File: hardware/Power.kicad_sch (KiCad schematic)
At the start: 70 parts, among them J10 I2C, J3 ESTOP, J4 PWR, J5 Conn_ARM_JTAG_SWD_10, J7 FAN, J9 DEBUG, Q1 MMBT5401LT1G, Q2 PSMN4R8-100BSEJ, Q3 MMBT3904, Q5 PSMN4R8-100BSEJ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

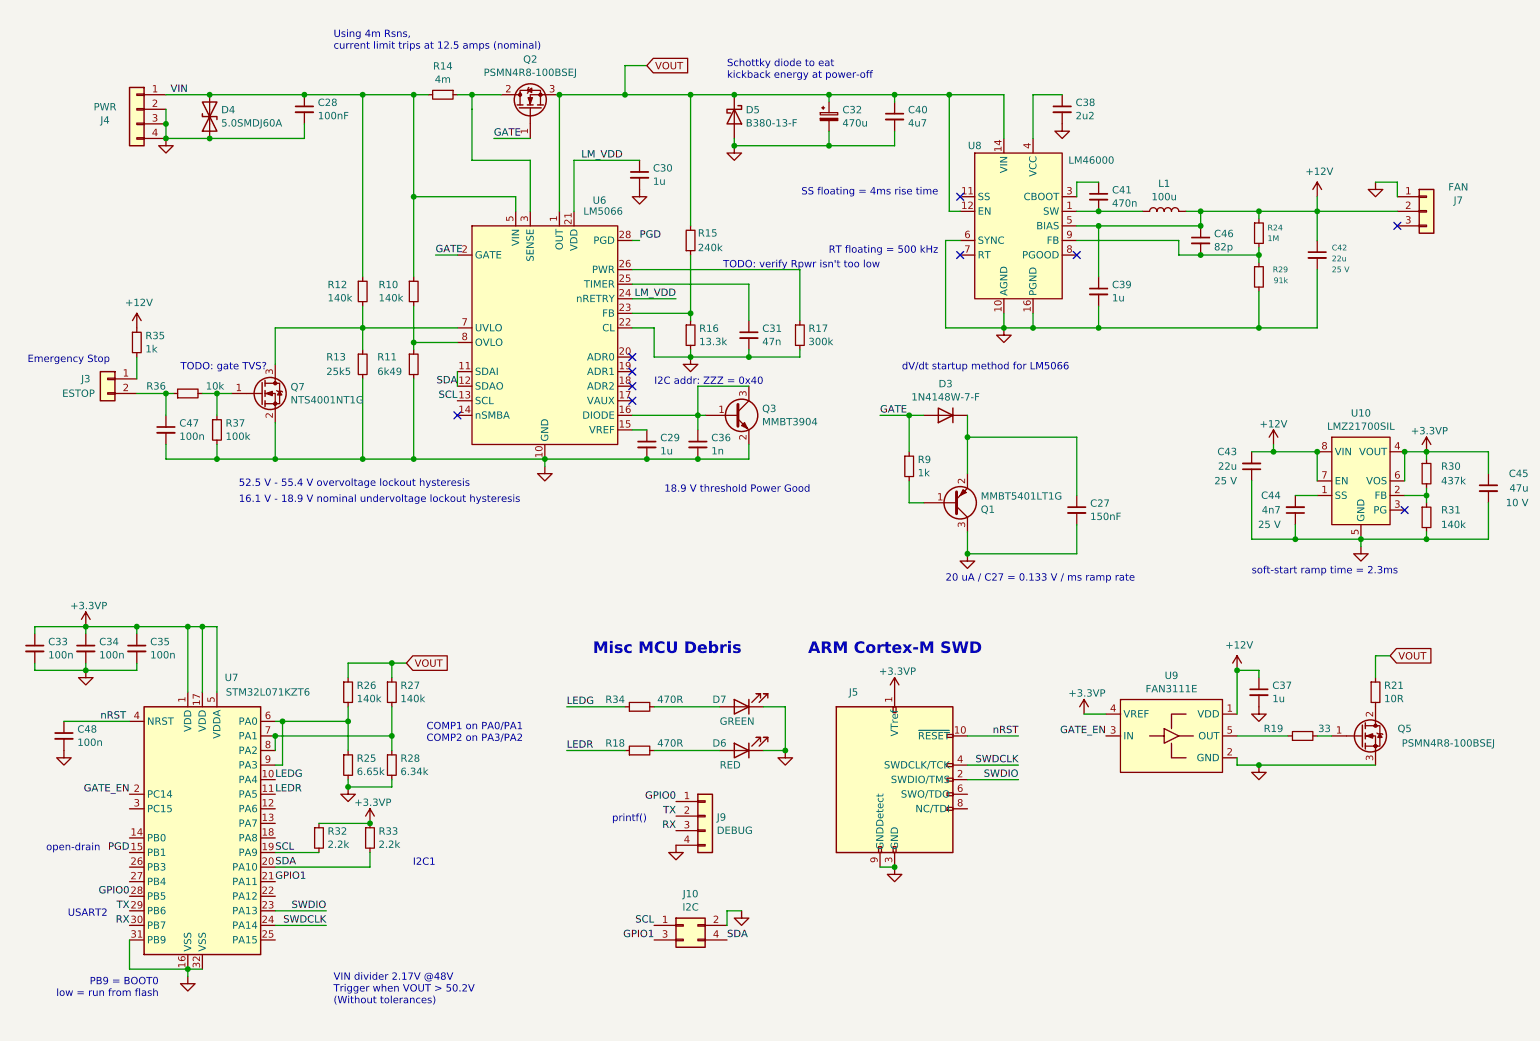
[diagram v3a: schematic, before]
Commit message: 12V rail supplied off of VIN and Shunt EN switched to a clockable pin.
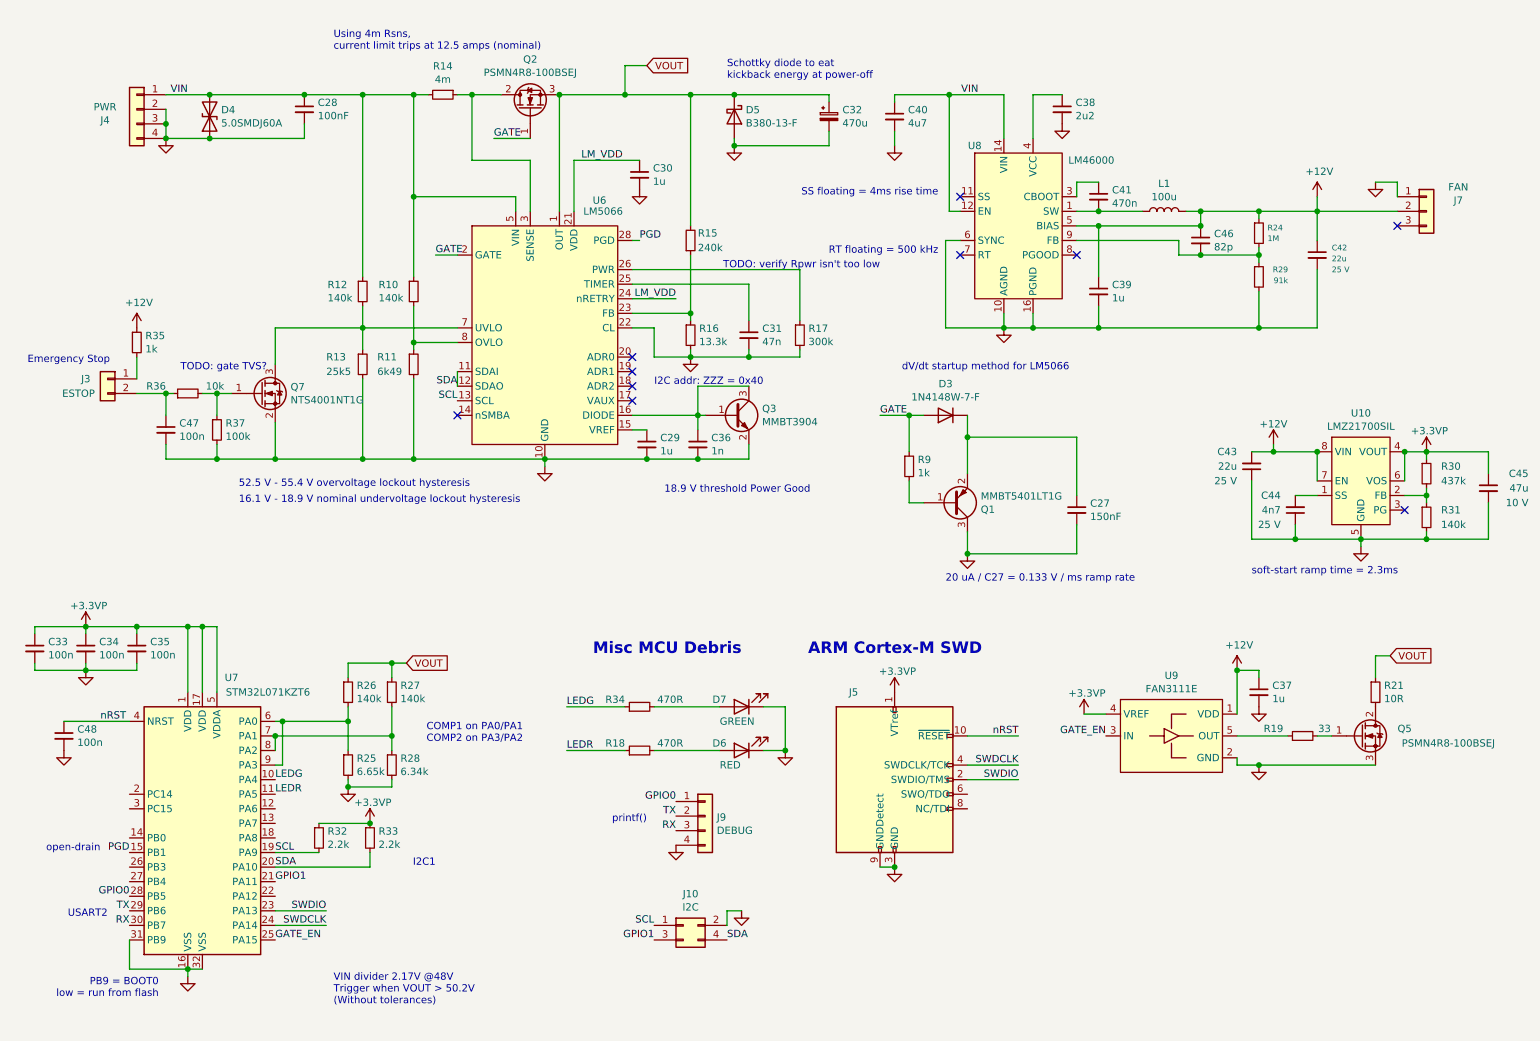
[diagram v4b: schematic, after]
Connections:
- net GATE_EN: now also U7.25 (PA15); no longer U7.2 (PC14)
- net VIN: now also C40.1, U8.12 (EN), U8.13 (VIN), U8.14 (VIN)
- net VOUT: no longer C40.1, U8.12 (EN), U8.13 (VIN), U8.14 (VIN)
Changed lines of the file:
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@@
   (junction (at 140.97 73.66) (diameter 1.016) (color 0 0 0 0))
   (junction (at 147.32 142.24) (diameter 1.016) (color 0 0 0 0))
-  (junction (at 154.94 27.94) (diameter 1.016) (color 0 0 0 0))
-  (junction (at 154.94 36.83) (diameter 1.016) (color 0 0 0 0))
-  (junction (at 166.37 27.94) (diameter 1.016) (color 0 0 0 0))
   (junction (at 166.37 162.56) (diameter 1.016) (color 0 0 0 0))
   (junction (at 168.91 83.82) (diameter 1.016) (color 0 0 0 0))
@@
   (junction (at 259.08 97.79) (diameter 1.016) (color 0 0 0 0))
   (junction (at 259.08 105.41) (diameter 1.016) (color 0 0 0 0))
-  (no_connect (at 254 50.8))
   (no_connect (at 90.17 83.82))
   (no_connect (at 255.27 100.33))
+  (no_connect (at 177.8 55.88))
+  (no_connect (at 254 50.8))
+  (no_connect (at 177.8 45.72))
   (no_connect (at 198.12 55.88))
   (no_connect (at 120.65 73.66))
+  (no_connect (at 120.65 78.74))
   (no_connect (at 120.65 76.2))
   (no_connect (at 120.65 81.28))
-  (no_connect (at 120.65 78.74))
-  (no_connect (at 177.8 55.88))
-  (no_connect (at 177.8 45.72))
   (wire (pts (xy 16.51 120.65) (xy 25.4 120.65))
     (stroke (width 0) (type solid) (color 0 0 0 0))
@@
     (stroke (width 0) (type solid) (color 0 0 0 0))
   )
-  (wire (pts (xy 92.71 27.94) (xy 92.71 30.48))
+  (wire (pts (xy 92.71 27.94) (xy 92.71 39.37))
     (stroke (width 0) (type solid) (color 0 0 0 0))
   )
@@
     (stroke (width 0) (type solid) (color 0 0 0 0))
   )
-  (wire (pts (xy 92.71 30.48) (xy 92.71 39.37))
-    (stroke (width 0) (type solid) (color 0 0 0 0))
-  )
   (wire (pts (xy 92.71 39.37) (xy 102.87 39.37))
     (stroke (width 0) (type solid) (color 0 0 0 0))
@@
     (stroke (width 0) (type solid) (color 0 0 0 0))
   )
-  (wire (pts (xy 154.94 27.94) (xy 166.37 27.94))
-    (stroke (width 0) (type solid) (color 0 0 0 0))
-  )
   (wire (pts (xy 154.94 34.29) (xy 154.94 36.83))
     (stroke (width 0) (type solid) (color 0 0 0 0))
@@
     (stroke (width 0) (type solid) (color 0 0 0 0))
   )
-  (wire (pts (xy 154.94 36.83) (xy 166.37 36.83))
-    (stroke (width 0) (type solid) (color 0 0 0 0))
-  )
   (wire (pts (xy 163.83 162.56) (xy 166.37 162.56))
     (stroke (width 0) (type solid) (color 0 0 0 0))
@@
     (stroke (width 0) (type solid) (color 0 0 0 0))
   )
+  (wire (pts (xy 175.895 27.94) (xy 175.895 48.26))
+    (stroke (width 0) (type solid) (color 0 0 0 0))
+  )
   (wire (pts (xy 175.895 27.94) (xy 185.42 27.94))
-    (stroke (width 0) (type solid) (color 0 0 0 0))
-  )
-  (wire (pts (xy 175.895 48.26) (xy 175.895 27.94))
     (stroke (width 0) (type solid) (color 0 0 0 0))
   )
@@
     (effects (font (size 1.27 1.27)) (justify left bottom))
   )
-  (label "GATE_EN" (at 33.02 149.86 180)
-    (effects (font (size 1.27 1.27)) (justify right bottom))
-  )
   (label "PGD" (at 33.02 160.02 180)
     (effects (font (size 1.27 1.27)) (justify right bottom))
@@
     (effects (font (size 1.27 1.27)) (justify left bottom))
   )
+  (label "GATE_EN" (at 58.42 175.26 0)
+    (effects (font (size 1.27 1.27)) (justify left bottom))
+  )
   (label "SWDIO" (at 67.31 170.18 180)
     (effects (font (size 1.27 1.27)) (justify right bottom))
@@
   (label "GATE" (at 163.83 83.82 0)
     (effects (font (size 1.27 1.27)) (justify left bottom))
+  )
+  (label "VIN" (at 180.975 27.94 180)
+    (effects (font (size 1.27 1.27)) (justify right bottom))
   )
   (label "nRST" (at 187.96 139.7 180)
@@
       (effects (font (size 1.27 1.27)) hide)
     )
+  )
+  (symbol (lib_id "power:GND") (at 166.37 36.83 0) (mirror y) (unit 1)
+    (in_bom yes) (on_board yes)
+    (property "Reference" "#PWR?" (id 0) (at 166.37 43.18 0)
+      (effects (font (size 1.27 1.27)) hide)
+    )
+    (property "Value" "GND" (id 1) (at 166.243 41.2242 0)
+      (effects (font (size 1.27 1.27)) hide)
+    )
+    (property "Footprint" "" (id 2) (at 166.37 36.83 0)
+      (effects (font (size 1.27 1.27)) hide)
+    )
+    (property "Datasheet" "" (id 3) (at 166.37 36.83 0)
+      (effects (font (size 1.27 1.27)) hide)
+    )

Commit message: Fix component sizing mistake (0402 -> 0603)
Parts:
- R29: D1PN 311-91.0KLRCT-ND -> 311-91.0KHRDKR-ND; MPN RC0402FR-0791KL -> RC0603FR-0791KL
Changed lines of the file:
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@@
   (junction (at 259.08 105.41) (diameter 1.016) (color 0 0 0 0))
   (no_connect (at 90.17 83.82))
+  (no_connect (at 177.8 45.72))
+  (no_connect (at 120.65 73.66))
+  (no_connect (at 254 50.8))
+  (no_connect (at 198.12 55.88))
+  (no_connect (at 120.65 81.28))
+  (no_connect (at 177.8 55.88))
   (no_connect (at 255.27 100.33))
-  (no_connect (at 177.8 55.88))
-  (no_connect (at 254 50.8))
-  (no_connect (at 177.8 45.72))
-  (no_connect (at 198.12 55.88))
-  (no_connect (at 120.65 73.66))
+  (no_connect (at 120.65 76.2))
   (no_connect (at 120.65 78.74))
-  (no_connect (at 120.65 76.2))
-  (no_connect (at 120.65 81.28))
   (wire (pts (xy 16.51 120.65) (xy 25.4 120.65))
     (stroke (width 0) (type solid) (color 0 0 0 0))
@@
       (effects (font (size 1.27 1.27)) hide)
     )
-    (property "D1PN" "311-91.0KLRCT-ND" (id 5) (at 233.4768 56.2102 0)
+    (property "D1PN" "311-91.0KHRDKR-ND" (id 5) (at 233.4768 56.2102 0)
       (effects (font (size 1.27 1.27)) hide)
     )
@@
       (effects (font (size 1.27 1.27)) hide)
     )
-    (property "MPN" "RC0402FR-0791KL" (id 7) (at 233.4768 56.2102 0)
-      (effects (font (size 1.27 1.27)) hide)
-    )
+    (property "MPN" "RC0603FR-0791KL" (id 7) (at 233.4768 56.2102 0)
+      (effects (font (size 1.27 1.27)) hide)
+    )
